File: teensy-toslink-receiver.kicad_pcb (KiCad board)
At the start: 2 copper layers, 24.9 x 18.3 mm, 11 parts, among them J1 Conn_01x03, J2 Conn_01x05, J3 Conn_01x05, J4 Conn_01x05, J5 Conn_01x03, J6 Conn_01x04, J7 HDMI_A_1.4, U1 PLR135-T10

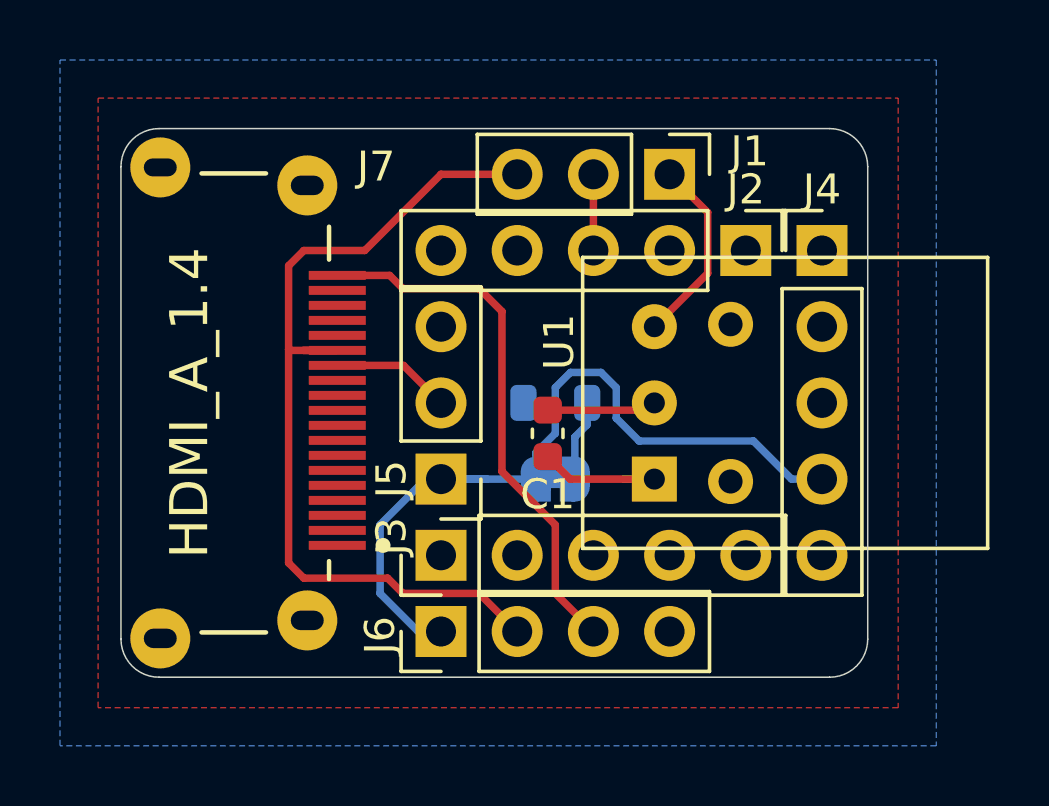
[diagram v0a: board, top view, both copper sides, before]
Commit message: pcb: Fix incorrectly placed Teensy headers and move connectors to bottom
* Headers were on inside when they should be on the outside. Oops.
* HDMI and TOSLINK connectors moved to bottom to prevent blocking teensy
  reset button.
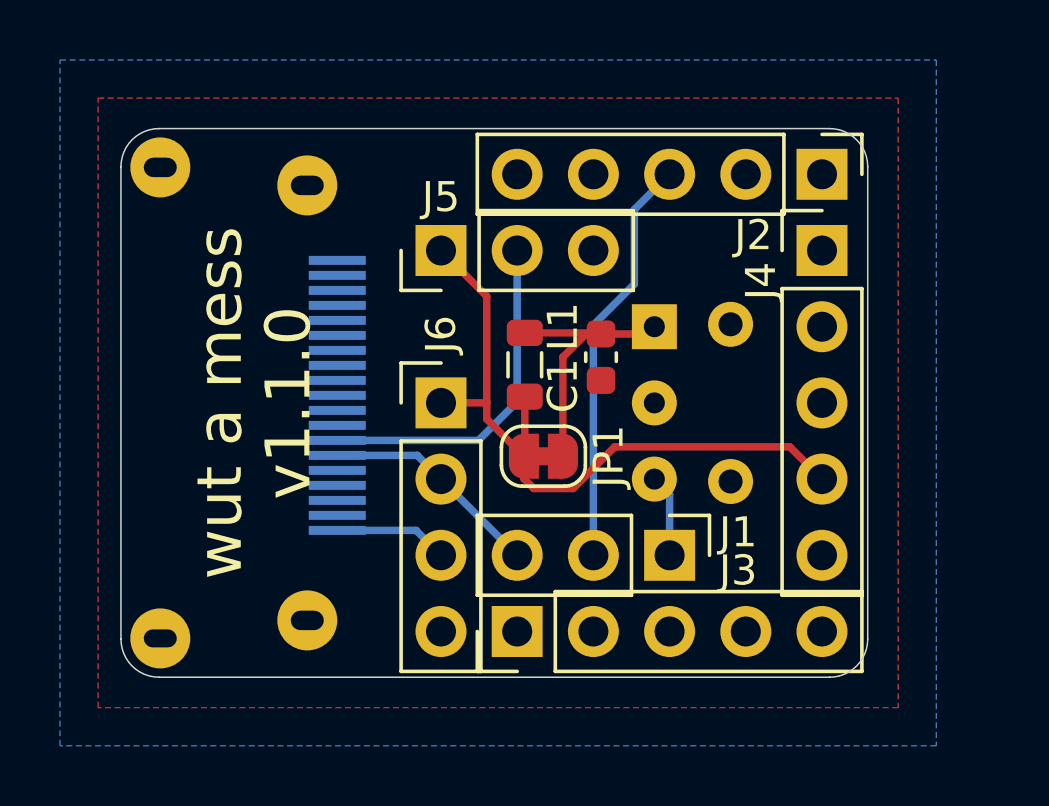
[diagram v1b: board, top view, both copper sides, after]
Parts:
- J7, U1: moved to B.Cu
- JP1, L1: moved to F.Cu
- moved J1 12.7 mm to (152.4, 78.7)
- moved J5 7.62 mm to (144.8, 68.6), turned to 90 degrees
- moved J6 7.62 mm to (144.8, 73.7), turned to 0 degrees
- moved J3 3.59 mm to (147.3, 81.3)
- moved J2 3.59 mm to (157.5, 66.0)
- moved C1 3.10 mm to (150.1, 72.1), turned to 270 degrees
- moved L1 1.63 mm to (147.6, 72.4), turned to 90 degrees
- moved JP1 0.86 mm to (148.2, 75.4)
- turned J7 to 90 degrees
- turned U1 to 90 degrees
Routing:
- net /ARC: track 30.1 -> 7.38 mm
- net /HPD: track 17.9 -> 3.80 mm
- net /SPDIF_IN: track 2.54 -> 14.3 mm
- net /CEC: track 3.97 -> 11.6 mm
- net +3V3: track 27.9 -> 23.4 mm
- net /TOSLINK_RX: track 6.85 -> 2.75 mm
- net GND: track 3.66 -> 0.35 mm
- net Net-(C1-Pad1): track 10.2 -> 9.73 mm
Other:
- board text added: "v1.1.0"

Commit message: pcb: Update PCB with new components
* Tighten up tolerances with OSH Park rules for 0603 components.
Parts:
- added Q1: BSS138, Package_TO_SOT_SMD:SOT-23, F.Cu at (141.2, 78.0)
- added Q2: BSS138, Package_TO_SOT_SMD:SOT-23, F.Cu at (137.7, 76.5)
- added Q3: BSS138, Package_TO_SOT_SMD:SOT-23, F.Cu at (137.7, 72.9)
- added R1: 27k, Resistor_SMD:R_0201_0603Metric, B.Cu at (143.5, 77.3)
- added R2: 0, Resistor_SMD:R_0201_0603Metric, F.Cu at (140.7, 74.7)
- added R3: 27k, Resistor_SMD:R_0201_0603Metric, F.Cu at (140.7, 75.4)
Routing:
- net /DIO9: track 0.00 -> 20.4 mm
- net /DIO17: track 0.00 -> 13.2 mm
- net +5V: track 0.00 -> 12.7 mm, vias 0 -> 1
- net /DIO8: track 0.00 -> 10.0 mm
- net /CEC: track 11.6 -> 17.2 mm, vias 0 -> 1
- net /HPD: track 3.80 -> 7.29 mm
- net GND: track 0.35 -> 3.71 mm, vias 0 -> 1
- net +3V3: track 23.4 -> 26.6 mm
- net Net-(Q2-Pad2): track 0.00 -> 2.52 mm
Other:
- net class Default: clearance 0.2 -> 0.1524; via_dia 0.8 -> 0.508; via_drill 0.4 -> 0.254
- rule trace_clearance: 0.2 -> 0.1524
- rule trace_min: 0.2 -> 0.1524
- rule via_min_drill: 0.3 -> 0.254
- rule via_min_size: 0.4 -> 0.508
